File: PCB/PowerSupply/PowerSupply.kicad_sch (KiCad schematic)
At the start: 18 parts, among them J1 Conn_01x03, U1 PinHeader, U2 Tactile-Switch, U3 Tactile-Switch, U4 ESP32-C6-MINI-1-N4, U5 BidirectionalLogicLevelShifter, U6 LinearVoltageRegulator, U7 USB-TypeC, U8 BidirectionalLogicLevelShifter

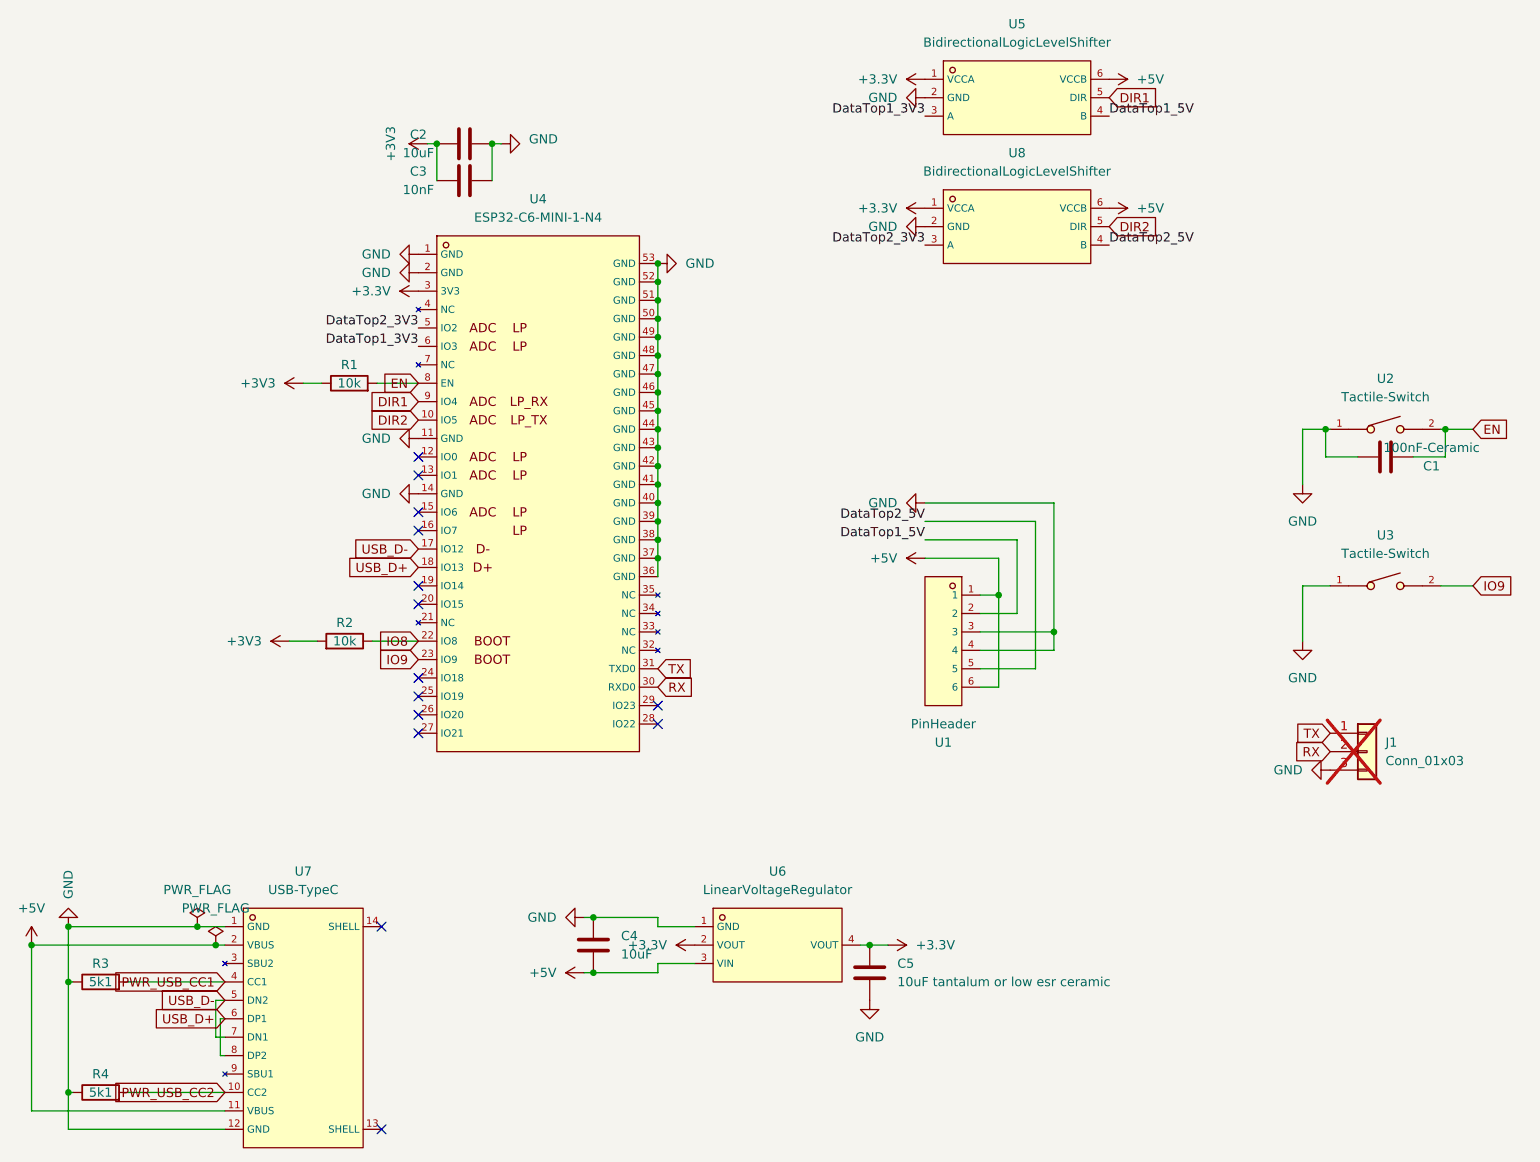
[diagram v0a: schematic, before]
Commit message: Finish module, power supply and connector design, panel is wip
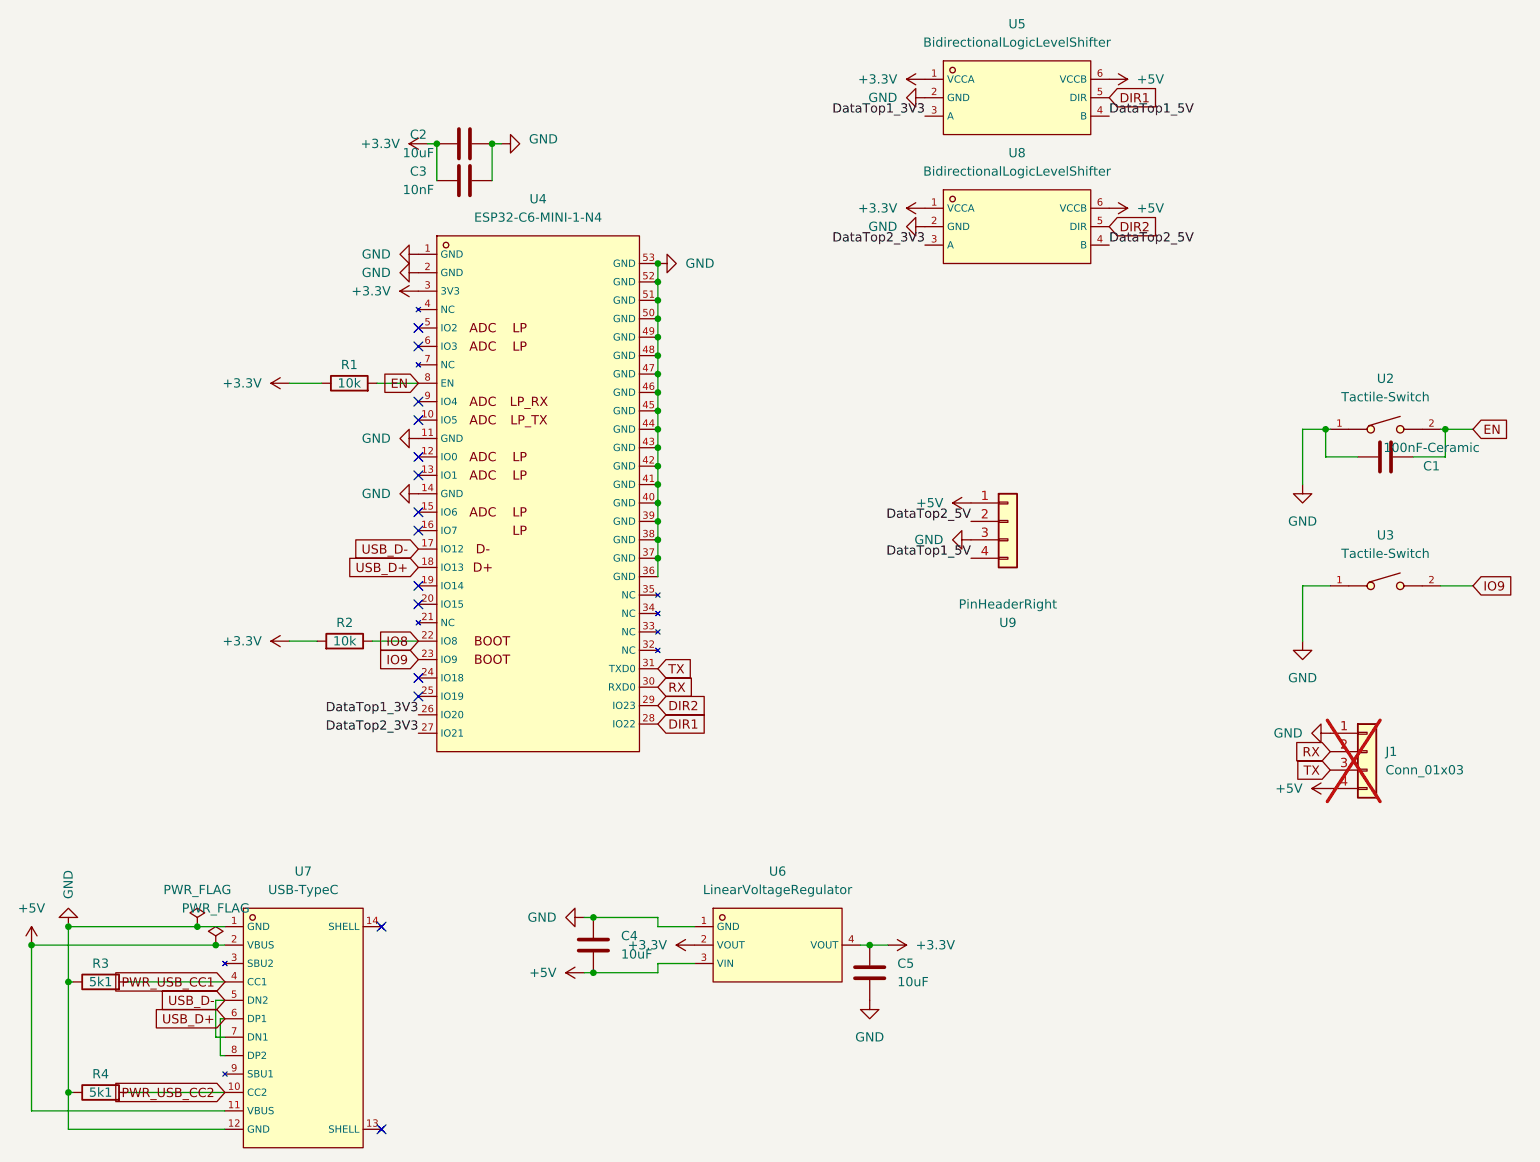
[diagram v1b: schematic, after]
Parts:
- removed U1: PinHeader, CustomFootprints:01x06_PinHeader_Angled, symbol Custom_Parts:01x06_PinHeader_Angled
- added U9: PinHeaderRight, CustomFootprints:01x04_PinPads, symbol Connector_Generic:Conn_01x04
- C2: LCSC C15525 -> C19702
- C4: LCSC (none) -> C19702
- C5: value 10uF tantalum or low esr ceramic -> 10uF; LCSC (none) -> C19702
- J1: footprint Connector_PinHeader_2.54mm:PinHeader_1x03_P2.54mm_Vertical -> Connector_PinHeader_2.54mm:PinHeader_1x04_P2.54mm_Vertical; symbol Connector_Generic:Conn_01x03 -> Connector_Generic:Conn_01x04; now in the parts list
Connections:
- net +3V3 is gone; now on net +3.3V: C2.1, C3.1, R1.1, R2.2
- net +5V: now also J1.4 (Pin_4), U9.1 (Pin_1)
- net DIR1: now also U4.28 (IO22); no longer U4.9 (IO4)
- net DIR2: now also U4.29 (IO23); no longer U4.10 (IO5)
- net DataTop1_3V3: now also U4.26 (IO20); no longer U4.6 (IO3)
- net DataTop1_5V: now also U9.4 (Pin_4)
- net DataTop2_3V3: now also U4.27 (IO21); no longer U4.5 (IO2)
- net DataTop2_5V: now also U9.2 (Pin_2)
- net GND: now also J1.1 (Pin_1), U9.3 (Pin_3); no longer J1.3 (Pin_3)
- net TX: now also J1.3 (Pin_3); no longer J1.1 (Pin_1)

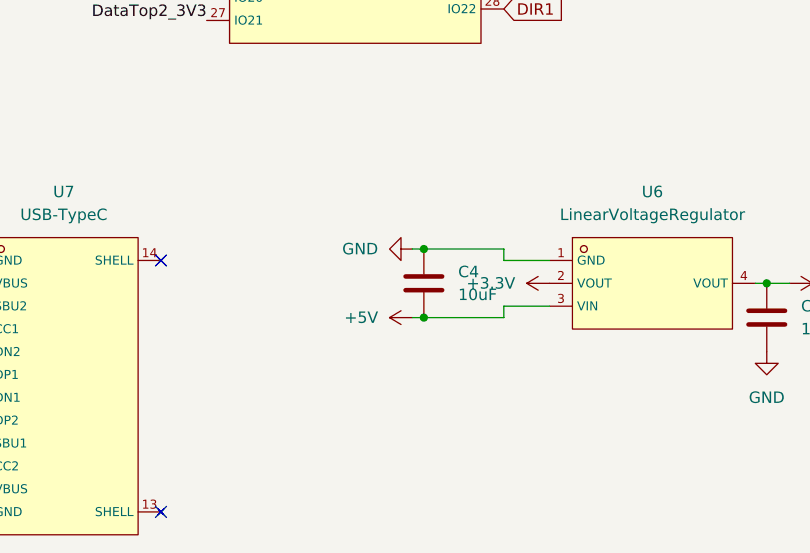
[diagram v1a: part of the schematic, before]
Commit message: Add electrolytic bulk capacitors to modules and power supply
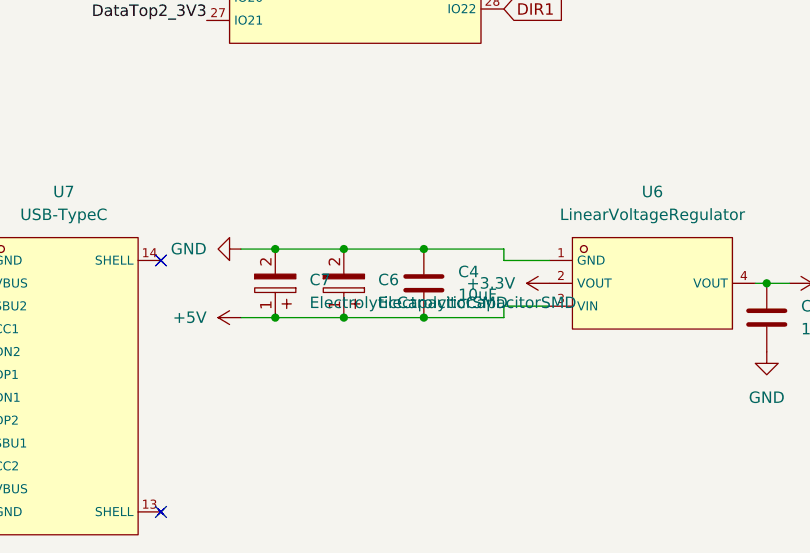
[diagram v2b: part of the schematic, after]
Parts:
- added C6, C7: ElectrolyticCapacitorSMD, CustomFootprints:CAP-SMD_BD6.3-L6.6-W6.6-FD, symbol Custom_Parts:ElectrolyticCapacitorSMD
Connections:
- net +5V: now also C6.1, C7.1
- net GND: now also C6.2, C7.2
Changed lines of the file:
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@@
 	)
 	(junction
+		(at 80.01 171.45)
+		(diameter 0)
+		(color 0 0 0 0)
+	)
+	(junction
 		(at 105.41 83.82)
 		(diameter 0)
@@
 	)
 	(junction
+		(at 87.63 163.83)
+		(diameter 0)
+		(color 0 0 0 0)
+	)
+	(junction
 		(at 105.41 96.52)
 		(diameter 0)
@@
 	)
 	(junction
+		(at 87.63 171.45)
+		(diameter 0)
+		(color 0 0 0 0)
+	)
+	(junction
+		(at 80.01 163.83)
+		(diameter 0)
+		(color 0 0 0 0)
+	)
+	(junction
 		(at 105.41 88.9)
 		(diameter 0)
@@
 	(wire
 		(pts
+			(xy 87.63 163.83) (xy 96.52 163.83)
+		)
+		(stroke
+			(width 0)
+			(type default)
+		)
+	)
+	(wire
+		(pts
 			(xy 105.41 101.6) (xy 105.41 104.14)
 		)
@@
 	(wire
 		(pts
+			(xy 87.63 171.45) (xy 96.52 171.45)
+		)
+		(stroke
+			(width 0)
+			(type default)
+		)
+	)
+	(wire
+		(pts
 			(xy 74.93 57.15) (xy 74.93 62.23)
 		)
@@
 	(wire
 		(pts
-			(xy 95.25 171.45) (xy 96.52 171.45)
+			(xy 76.2 171.45) (xy 80.01 171.45)
 		)
 		(stroke
@@
 	(wire
 		(pts
+			(xy 80.01 163.83) (xy 87.63 163.83)
+		)
+		(stroke
+			(width 0)
+			(type default)
+		)
+	)
+	(wire
+		(pts
 			(xy 45.085 177.8) (xy 45.72 177.8)
 		)
@@
 	(wire
 		(pts
+			(xy 80.01 171.45) (xy 87.63 171.45)
+		)
+		(stroke
+			(width 0)
+			(type default)
+		)
+	)
+	(wire
+		(pts
 			(xy 24.13 172.72) (xy 24.765 172.72)
 		)
@@
 	(wire
 		(pts
-			(xy 95.25 163.83) (xy 96.52 163.83)
+			(xy 76.2 163.83) (xy 80.01 163.83)
 		)
 		(stroke
@@
 	(symbol
 		(lib_id "power:+5V")
-		(at 95.25 171.45 90)
+		(at 76.2 171.45 90)
 		(unit 1)
 		(exclude_from_sim no)
@@
 		(fields_autoplaced yes)
 		(property "Reference" "#PWR9"
-			(at 99.06 171.45 0)
+			(at 80.01 171.45 0)
 			(effects
 				(font
@@
 		)
 		(property "Value" "+5V"
-			(at 91.44 171.4499 90)
+			(at 72.39 171.4499 90)
 			(effects
 				(font
@@
 		)
 		(property "Footprint" ""
-			(at 95.25 171.45 0)
+			(at 76.2 171.45 0)
 			(effects
 				(font
@@
 		)
 		(property "Datasheet" ""
-			(at 95.25 171.45 0)
+			(at 76.2 171.45 0)
 			(effects
 				(font
@@
 		)
 		(property "Description" "Power symbol creates a global label with name \"+5V\""
-			(at 95.25 171.45 0)
+			(at 76.2 171.45 0)
 			(effects
 				(font
@@
 	)
 	(symbol
+		(lib_id "Custom_Parts:ElectrolyticCapacitorSMD")
+		(at 87.63 167.64 180)
+		(unit 1)
+		(exclude_from_sim no)
+		(in_bom yes)
+		(on_board yes)
+		(dnp no)
+		(fields_autoplaced yes)
+		(property "Reference" "C6"
+			(at 91.44 167.2589 0)
+			(effects
+				(font
+					(size 1.27 1.27)
+				)
+				(justify right)
+			)
+		)
+		(property "Value" "ElectrolyticCapacitorSMD"
+			(at 91.44 169.7989 0)
+			(effects
+				(font
+					(size 1.27 1.27)
+				)
+				(justify right)
+			)
+		)
+		(property "Footprint" "CustomFootprints:CAP-SMD_BD6.3-L6.6-W6.6-FD"
+			(at 87.63 157.48 0)
+			(effects
+				(font
+					(size 1.27 1.27)
+					(italic yes)
+				)
+				(hide yes)
+			)
+		)
+		(property "Datasheet" "https://item.szlcsc.com/265679.html"
+			(at 89.916 167.767 0)
+			(effects
+				(font
+					(size 1.27 1.27)
+				)
+				(justify left)
+				(hide yes)
+			)
+		)
+		(property "Description" ""
+			(at 87.63 167.64 0)
+			(effects
+				(font
+					(size 1.27 1.27)
+				)
+				(hide yes)
+			)
+		)
+		(property "LCSC" "C335982"
+			(at 87.63 167.64 0)
+			(effects
+				(font
+					(size 1.27 1.27)
+				)
+				(hide yes)
+			)
+		)
+		(pin "1"
+		)
+		(pin "2"
+		)
+		(instances
+			(project ""
+				(path "/31a90a99-29a4-42c9-bd5d-1c649e11c1d3"
+					(reference "C6")
+					(unit 1)
+				)
+			)
+		)
+	)
+	(symbol
 		(lib_id "power:+5V")
 		(at 167.64 66.04 270)
@@
 	(symbol
 		(lib_id "power:GND")
-		(at 95.25 163.83 270)
+		(at 76.2 163.83 270)
 		(unit 1)
 		(exclude_from_sim no)
@@
 		(fields_autoplaced yes)
 		(property "Reference" "#PWR12"
-			(at 88.9 163.83 0)
+			(at 69.85 163.83 0)
 			(effects
 				(font
@@
 		)
 		(property "Value" "GND"
-			(at 91.44 163.8299 90)
+			(at 72.39 163.8299 90)
 			(effects
 				(font
@@
 		)
 		(property "Footprint" ""
-			(at 95.25 163.83 0)
+			(at 76.2 163.83 0)
 			(effects
 				(font
@@
 		)
 		(property "Datasheet" ""
-			(at 95.25 163.83 0)
+			(at 76.2 163.83 0)
 			(effects
 				(font
@@
 		)
 		(property "Description" "Power symbol creates a global label with name \"GND\" , ground"
-			(at 95.25 163.83 0)
+			(at 76.2 163.83 0)
 			(effects
 				(font
@@
 					(unit 1)
 				)
+			)
+		)
+	)
+	(symbol
+		(lib_id "Custom_Parts:ElectrolyticCapacitorSMD")
+		(at 80.01 167.64 180)
+		(unit 1)
+		(exclude_from_sim no)
+		(in_bom yes)
+		(on_board yes)
+		(dnp no)
+		(fields_autoplaced yes)
+		(property "Reference" "C7"
+			(at 83.82 167.2589 0)
+			(effects
+				(font
+					(size 1.27 1.27)
+				)
+				(justify right)
+			)
+		)
+		(property "Value" "ElectrolyticCapacitorSMD"
+			(at 83.82 169.7989 0)
+			(effects
+				(font
+					(size 1.27 1.27)
+				)
+				(justify right)
+			)
+		)
+		(property "Footprint" "CustomFootprints:CAP-SMD_BD6.3-L6.6-W6.6-FD"
+			(at 80.01 157.48 0)
+			(effects
+				(font
+					(size 1.27 1.27)
+					(italic yes)
+				)
+				(hide yes)
+			)
+		)
+		(property "Datasheet" "https://item.szlcsc.com/265679.html"
+			(at 82.296 167.767 0)
+			(effects
+				(font
+					(size 1.27 1.27)
+				)
+				(justify left)
+				(hide yes)
+			)
+		)
+		(property "Description" ""
+			(at 80.01 167.64 0)
+			(effects
+				(font
+					(size 1.27 1.27)
+				)
+				(hide yes)
+			)
+		)
+		(property "LCSC" "C335982"
+			(at 80.01 167.64 0)
+			(effects
+				(font
+					(size 1.27 1.27)
+				)
+				(hide yes)
+			)
+		)
+		(pin "1"
+		)
+		(pin "2"
+		)
+		(instances
+			(project "PowerSupply"
+				(path "/31a90a99-29a4-42c9-bd5d-1c649e11c1d3"
+					(reference "C7")
+					(unit 1)
+				)
